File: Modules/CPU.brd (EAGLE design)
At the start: 132.1 x 55.5 mm, 89 parts, among them IC4 93LC66SM, IC5 MIC2026-1YM, J1 USB_A_SMT_FEMALE, J2 USB_A_SMT_FEMALE, J4 SD_CARD_SOCKET, Q1 DMG1012T-7, Q2 DMG1012T-7, Q3 DMG1012T-7, U5 LAN9512-JZX, U6 FSUSB42UMX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

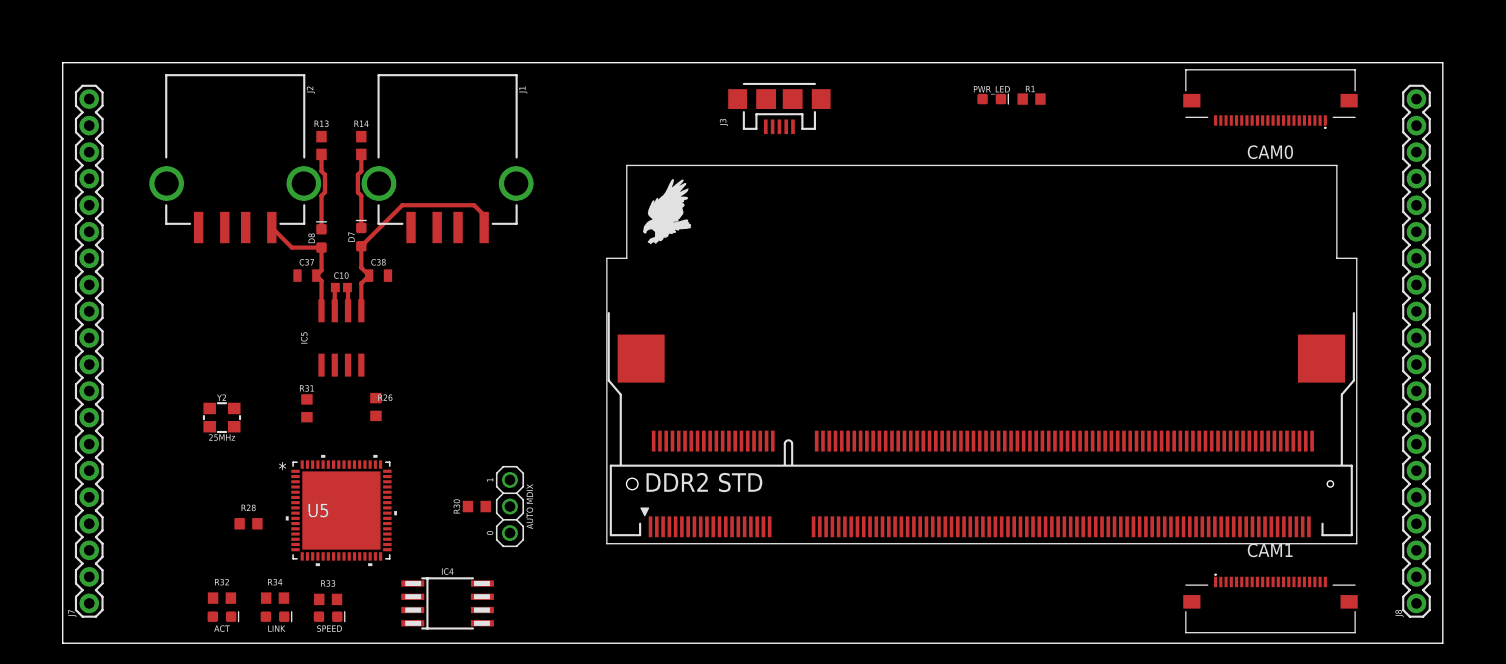
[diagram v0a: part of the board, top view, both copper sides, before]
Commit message: Updated CPU Module and Added Module to Library
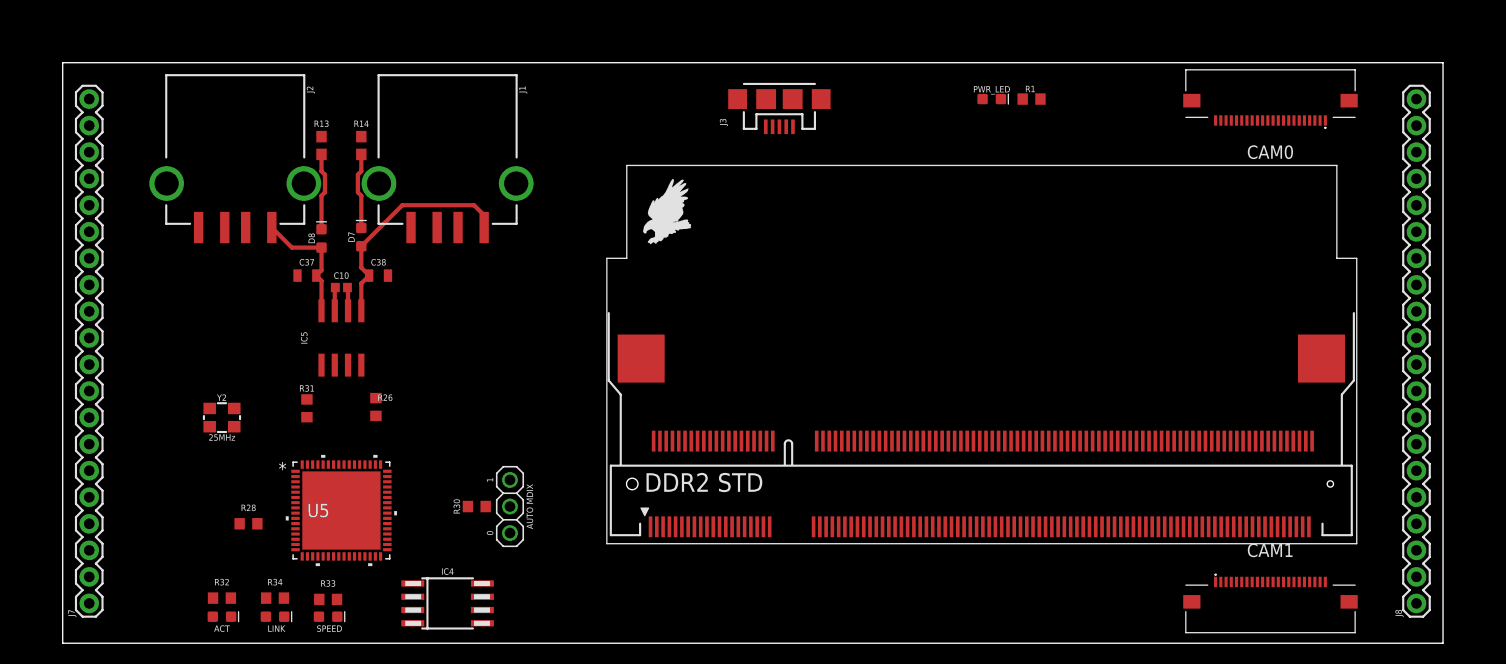
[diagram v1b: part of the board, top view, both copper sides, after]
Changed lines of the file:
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@@
 <?xml version="1.0" encoding="utf-8"?>
 <!DOCTYPE eagle SYSTEM "eagle.dtd">
-<eagle version="9.3.0">
+<eagle version="9.2.2">
 <drawing>
 <settings>
@@
 <board>
 <plain>
-<wire x1="0" y1="0" x2="132.06" y2="0" width="0" layer="20"/>
-<wire x1="132.06" y1="0" x2="132.06" y2="55.55" width="0" layer="20"/>
-<wire x1="132.06" y1="55.55" x2="0" y2="55.55" width="0" layer="20"/>
-<wire x1="0" y1="55.55" x2="0" y2="0" width="0" layer="20"/>
+<wire x1="0" y1="0" x2="132.08" y2="0" width="0" layer="20"/>
+<wire x1="132.08" y1="0" x2="132.08" y2="55.5498" width="0" layer="20"/>
+<wire x1="132.08" y1="55.5498" x2="0" y2="55.5498" width="0" layer="20"/>
+<wire x1="0" y1="55.5498" x2="0" y2="0" width="0" layer="20"/>
 <text x="20.447" y="1.397" size="0.6096" layer="25" font="vector" ratio="20" align="center">LINK</text>
 <text x="25.527" y="1.397" size="0.6096" layer="25" font="vector" ratio="20" align="center">SPEED</text>
